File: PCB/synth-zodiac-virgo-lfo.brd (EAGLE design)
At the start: 160 x 100 mm, 30 parts, among them Q10 PNP, Q11 NPN, Q9 PNP, SW7 SPDT, U11 TL074A, U12 LM13700, U9 TL072A

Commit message: Snapshot of designs so far.
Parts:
- removed C37, C38: 0.1uF, rlc:0603-CAP
- removed LED1: RED, led:THD_3MM
- removed SW7: SPDT, switch-thd:SS-12-F45
- removed U9: TL072A, op-amp:SOP08
- removed VR11: 10K, rlc:ALPS_RK09D113
- added CONST1: Virgo, circuit-monkey-zodiac:VIRGO-CONST
- added CP_GND, CP_LFO_CV: PADSMD-070X070, con-testpoints:SMD-070MIL
- added GLYPH1: Virgo, circuit-monkey-zodiac:VIRGO-GLYPH
- added LED: BLU, led:SMD_0603
- added OUT_VCF, OUT_VCO: 2-pin, VT, SMT, con-jst:B2B-PH-SM4
- added PCB1: PCB FAB, circuit-monkey-zodiac:PENTAGON-40MM-RAD
- added PWR: (no value), con-jst:B4B-PH-SM4
- added RATE: 10K, rlc:POT-RV9110
- added WAVE: SPDT, switch-thd:SS-12-F45-PNL-SMT
- LFO_SQ, LFO_TRI: value TPTHD-038 -> TPSMD-040-RND; device con-testpoints:THD-038MIL-X1 -> con-testpoints:SMD-040MIL-RND
- moved C41 101.0 mm to (58.9, 44.1), flipped to the bottom
- moved C39 100.5 mm to (44.6, 45.5), flipped to the bottom, turned to 180 degrees
- moved C40 99.5 mm to (47.5, 45.5), flipped to the bottom, turned to 180 degrees
- moved C42 97.6 mm to (56.0, 44.1), flipped to the bottom
- moved LFO_TRI 95.9 mm to (44.0, 50.3), flipped to the bottom, turned to 180 degrees
- moved LFO_SQ 90.6 mm to (43.8, 48.0), flipped to the bottom
- moved R65 89.3 mm to (39.4, 43.3), flipped to the bottom
- moved R68 86.9 mm to (33.7, 37.9), flipped to the bottom
- moved R64 85.8 mm to (46.4, 33.2), flipped to the bottom
- moved R69 83.5 mm to (33.7, 36.6), flipped to the bottom, turned to 180 degrees
- moved R63 82.0 mm to (39.4, 41.9), flipped to the bottom, turned to 180 degrees
- moved R62 81.9 mm to (57.5, 32.0), flipped to the bottom
- moved R67 80.8 mm to (33.7, 39.2), flipped to the bottom
- moved C36 80.1 mm to (46.4, 30.6), flipped to the bottom
- moved R61 79.4 mm to (46.4, 31.9), flipped to the bottom, turned to 180 degrees
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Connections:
- removed net N$84: R63.2, U12.12, U12.14, U12.3, U9.5
- new net LFO_OSC: R63.2, U11.12, U12.12, U12.14, U12.3
- net +9V: now also LED.A, PWR.1, RATE.T; no longer C37.1, LED1.A, U9.8, VR11.3
- net -9V: now also PWR.2, RATE.B; no longer C38.2, U9.4, VR11.1
- net GND: now also CP_GND.1, OUT_VCF.2, OUT_VCO.2, PCB1.MTG1, PCB1.MTG2, PCB1.MTG3, PCB1.MTG4, PCB1.MTG5, PWR.4; no longer C37.2, C38.1, VR11.MT1A, VR11.MT1B, VR11.MT1C, VR11.MT2A, VR11.MT2B, VR11.MT2C
- net LFO_CV: now also OUT_VCF.1, OUT_VCO.1, WAVE.C; no longer SW7.C
- net LFO_CV_IN: now also CP_LFO_CV.1
- net LFO_SQ: now also LFO_SQ.TP, U11.13, U11.14, WAVE.B; no longer LFO_SQ.1, SW7.B, U9.6, U9.7
- net LFO_TRI: now also LFO_TRI.TP, U11.1, U11.2, WAVE.A; no longer LFO_TRI.1, SW7.A, U11.6, U11.7
- net N$76: now also RATE.C; no longer VR11.2
- net N$79: now also U11.10; no longer U9.3
- net N$80: now also U11.8, U11.9; no longer U9.1, U9.2
- net N$85: now also U11.3; no longer U11.5
- net N$91: now also LED.K; no longer LED1.K
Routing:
- net +9V: track 0.00 -> 153.6 mm, vias 0 -> 6
- net LFO_CV: track 0.00 -> 148.8 mm
- net -9V: track 0.00 -> 76.7 mm, vias 0 -> 2
- net LFO_TRI: track 0.00 -> 30.3 mm
- net N$85: track 0.00 -> 29.7 mm
- net LFO_SQ: track 0.00 -> 26.2 mm
- net LFO_OSC: track 0.00 -> 18.7 mm, vias 0 -> 2
- net N$76: track 0.00 -> 18.0 mm
- net N$82: track 0.00 -> 16.0 mm, vias 0 -> 2
- net LFO_CV_IN: track 0.00 -> 15.6 mm
- net N$79: track 0.00 -> 13.5 mm
- net N$90: track 0.00 -> 13.0 mm
- net N$83: track 0.00 -> 11.7 mm, vias 0 -> 3
- net N$80: track 0.00 -> 8.35 mm
- net N$89: track 0.00 -> 8.08 mm
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- added copper zone on layer 1, net GND
- added copper zone on layer 16, net GND
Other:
- board size 160 x 100 mm -> 76.1 x 72.4 mm
- board text added: "LFO"
- board text added: "SQ TRI"
- board text added: "V I R G O"

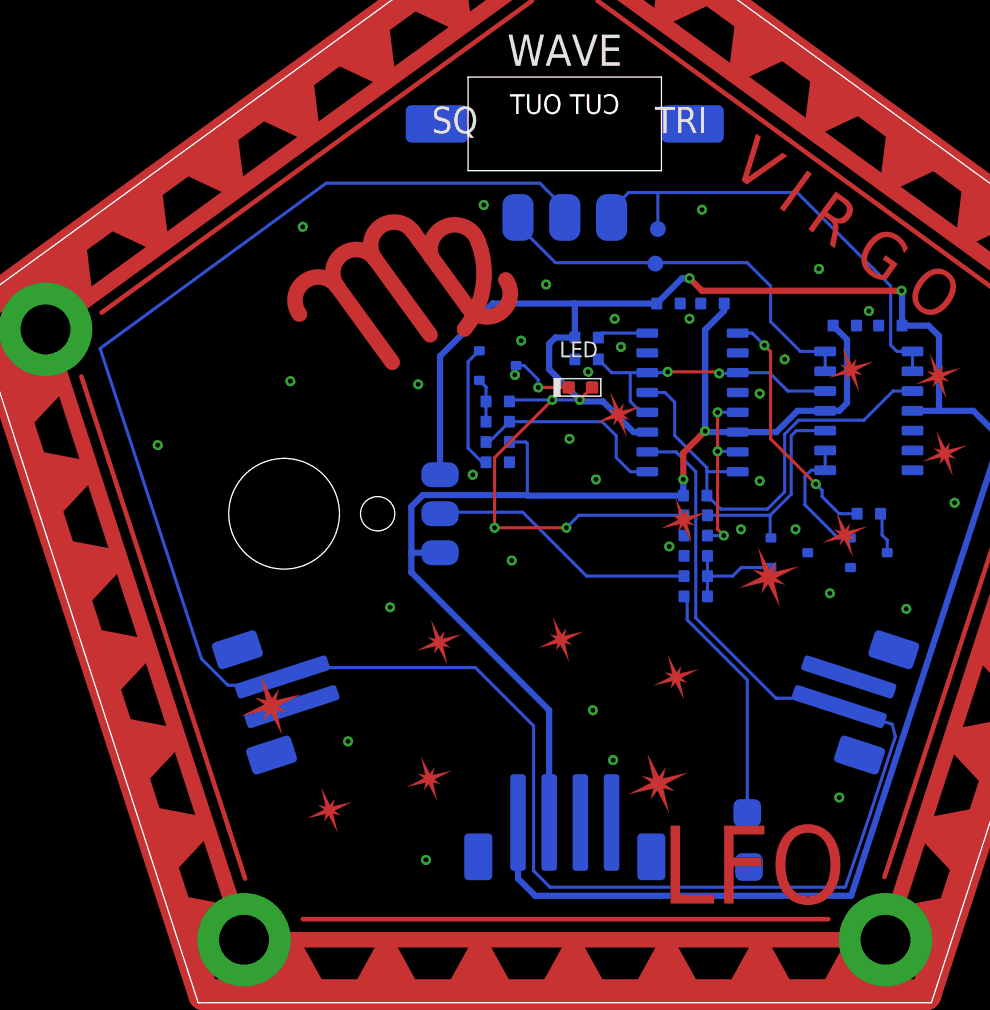
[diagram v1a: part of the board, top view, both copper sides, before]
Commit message: Almost ready for FAB.
Sagittarius was mis-spelled, renamed it.  Taurus is still WIP.
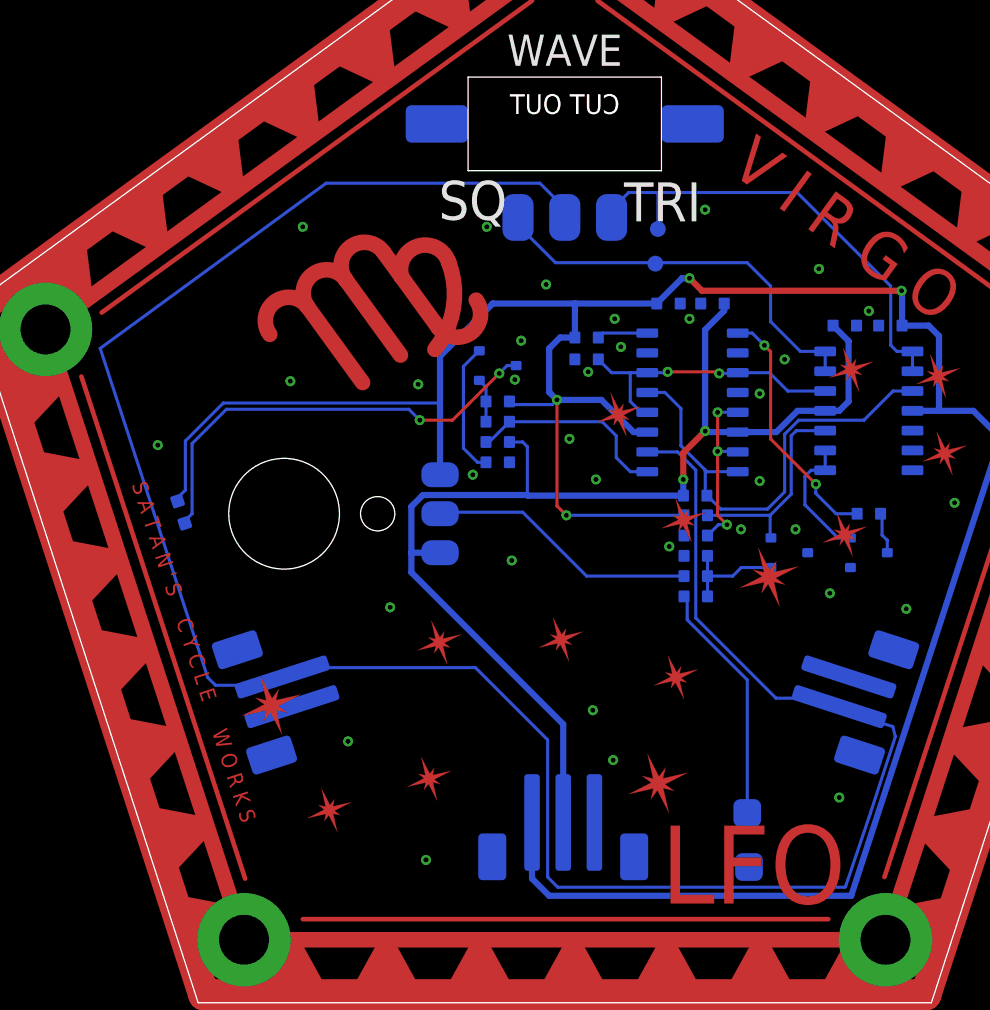
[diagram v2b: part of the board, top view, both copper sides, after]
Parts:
- PWR: value (none) -> JST, 3P, VT, SMT; device con-jst:B4B-PH-SM4 -> con-jst:B3B-PH-SM4
- moved LED 26.8 mm to (13.4, 32.1), flipped to the bottom, turned to 72 degrees
- moved GLYPH1 2.30 mm to (25.7, 44.6)
- moved PWR 0.10 mm to (37.9, 10.0)
- renumbered C36 to C1, C39 to C2, C40 to C3, C41 to C4, C42 to C5, OUT_VCF to 2VCF_MOD, OUT_VCO to 2VCO_MOD, Q11 to Q1, R58 to R2, R59 to R3, R60 to R1, R61 to R4, R62 to R5, R63 to R6, R64 to R7, R65 to R8, R66 to R12, R67 to R11, R68 to R10, R69 to R9, U11 to U1, U12 to U2
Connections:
- net GND: now also PWR.3; no longer PWR.4
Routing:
- net N$91: track 4.24 -> 28.7 mm, vias 1 -> 2
- net +9V: track 153.6 -> 165.2 mm, vias 6 -> 4
- net N$76: track 18.0 -> 17.4 mm
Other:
- board text added: "Rev. A"
- board text added: "S A T A N ' S C Y C L E W O R K S"
- board text added: "SQ"
- board text added: "TRI"
- board text removed: "SQ TRI"

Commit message: Work in progress for rev A,  VCO rev.B
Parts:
- removed CP_GND, CP_LFO_CV: PADSMD-070X070, con-testpoints:SMD-070MIL
- removed WAVE: SPDT, switch-thd:SS-12-F45-PNL-SMT
- added R13: 150K, rlc:0603-RES
- added R14: 47K, rlc:0603-RES
- added R_0-5, R_GND: PADSMD-070X070, con-testpoints:SMD-070MIL
- added TYPE: (no value), switch-thd:SS-12-F45-PNL-SMT
- 2VCF_MOD, 2VCO_MOD: value 2-pin, VT, SMT -> JST, SH, 2P; device con-jst:B2B-PH-SM4 -> con-jst:BM02B-SRSS-TB
- PWR: value JST, 3P, VT, SMT -> JST SM 3P; device con-jst:B3B-PH-SM4 -> con-jst:BM03B-SRSS-TB
- R1: value 221K -> 150K
- moved 2VCO_MOD 38.6 mm to (56.6, 22.2), turned to 108 degrees
- moved Q10 24.3 mm to (36.8, 42.2), turned to 270 degrees
- moved R5 22.1 mm to (36.8, 39.8), turned to 180 degrees
- moved R1 18.8 mm to (28.4, 21.3)
- moved R4 18.2 mm to (38.7, 15.4)
- moved Q9 17.7 mm to (39.1, 17.8), turned to 270 degrees
- moved R8 16.5 mm to (30.6, 29.4), turned to 180 degrees
- moved R6 14.2 mm to (30.6, 30.7)
- moved C2 12.6 mm to (35.4, 37.0)
- moved C3 12.6 mm to (38.2, 37.0)
- moved U2 12.4 mm to (36.8, 31.0)
- moved R3 10.6 mm to (39.3, 21.4)
- moved R2 10.6 mm to (39.3, 20.1)
- moved 2VCF_MOD 8.12 mm to (58.5, 28.0)
- moved U1 7.69 mm to (49.9, 37.4)
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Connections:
- removed net LFO_CV_IN: CP_LFO_CV.1, R1.1
- removed net N$76: R2.1, RATE.C
- new net RATE: R13.1, R2.1, RATE.C
- new net RATE_5: R1.1, R13.2, R14.2, R_0-5.1
- net +9V: now also R1.2
- net GND: now also R14.1, R_GND.1, U1.5, U1.6; no longer CP_GND.1
- net LFO_CV: now also TYPE.C; no longer WAVE.C
- net LFO_SQ: now also TYPE.B; no longer WAVE.B
- net LFO_TRI: now also TYPE.A; no longer WAVE.A
- net N$77: no longer R1.2
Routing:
- net LFO_CV: track 148.8 -> 88.2 mm, vias 0 -> 3
- net RATE: track 0.00 -> 36.9 mm, vias 0 -> 2
- net -9V: track 77.0 -> 107.2 mm, vias 2 -> 4
- net N$79: track 13.5 -> 42.7 mm, vias 0 -> 2
- net +9V: track 165.2 -> 136.7 mm
- net N$76: track 17.4 -> 0.00 mm
- net LFO_CV_IN: track 15.6 -> 0.00 mm
- net N$82: track 16.1 -> 6.06 mm, vias 2 -> 0
- net LFO_TRI: track 30.3 -> 21.3 mm
- net N$80: track 8.35 -> 15.3 mm
- net N$89: track 8.51 -> 1.77 mm
- net LFO_OSC: track 18.7 -> 25.2 mm, vias 2 -> 4
- net N$85: track 29.8 -> 34.9 mm, vias 0 -> 2
- net N$87: track 3.26 -> 8.29 mm
- net N$91: track 28.7 -> 24.1 mm, vias 2 -> 0
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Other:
- board text removed: "SQ"
- board text removed: "TRI"

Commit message: Perhaps final Rev. A?
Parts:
- TYPE: device switch-thd:SS-12-F45-PNL-SMT -> switch-thd:SS-12-F45-PNL-SMT-2
- flipped TYPE to the top
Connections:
- net LFO_SQ: now also TYPE.A; no longer TYPE.B
- net LFO_TRI: now also TYPE.B; no longer TYPE.A
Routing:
- net LFO_TRI: track 21.3 -> 23.3 mm
- net LFO_CV: track 88.2 -> 89.1 mm

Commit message: Tune values and some schematic visual tweaks.
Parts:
- R3: value 3.32 -> 3.32K
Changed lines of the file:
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@@
 <attribute name="VALUE" x="39.3" y="19.846" size="0.2" layer="28" rot="MR180" align="center"/>
 </element>
-<element name="R3" library="rlc" library_urn="urn:adsk.eagle:library:4192893" package="0603-RES" package3d_urn="urn:adsk.eagle:package:4193040/5" value="3.32" x="39.3" y="21.4" smashed="yes" rot="MR0">
+<element name="R3" library="rlc" library_urn="urn:adsk.eagle:library:4192893" package="0603-RES" package3d_urn="urn:adsk.eagle:package:4193040/5" value="3.32K" x="39.3" y="21.4" smashed="yes" rot="MR0">
 <attribute name="COST01" value="0.10" x="72.32" y="50.61" size="1.778" layer="28" rot="MR0" display="off"/>
 <attribute name="COST10" value="0.05" x="72.32" y="50.61" size="1.778" layer="28" rot="MR0" display="off"/>
